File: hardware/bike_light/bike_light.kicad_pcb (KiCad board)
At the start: 2 copper layers, 65 x 22 mm, 54 parts, among them J1 Battery, J2 USB_C_Receptacle_USB2.0_16P, SW1 SW_Push, SW2 SW_Push, U1 TPS22918DBV, U2 ESP32-C3-WROOM-02, U3 XC6220B331MR, U4 BQ21040DBV

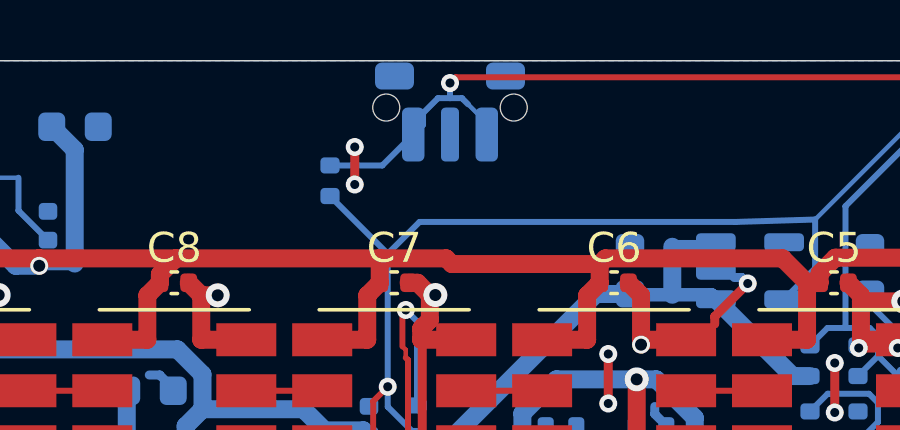
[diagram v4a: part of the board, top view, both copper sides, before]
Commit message: Moved button away from edge a bit
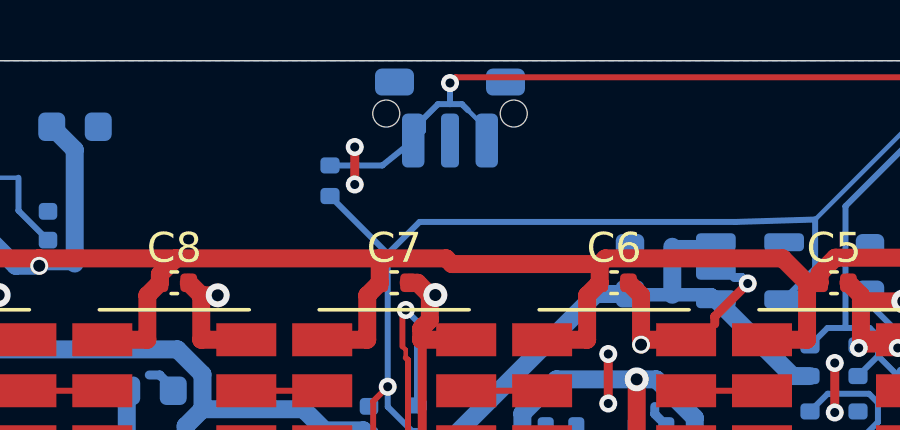
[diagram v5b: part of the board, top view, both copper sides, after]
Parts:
- moved SW1 0.20 mm to (128.0, 101.8)
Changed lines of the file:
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@@
 	(footprint "bike_light:SW_Push_1P1T-MP_NO_Horizontal_Alps_SKRTLAE010"
 		(layer "B.Cu")
-		(at 128 101.56)
+		(at 128 101.76)
 		(descr "Side push button (https://www.alps.com/prod/info/E/PDF/Tact/SurfaceMount/SKRT/SKRT.pdf)")
 		(tags "push horizontal SPST 1P1T")
@@
 	)
 	(segment
-		(start 125.625 114.275)
-		(end 125.275 114.625)
-		(width 0.3)
-		(layer "F.Cu")
-		(net "GND")
-	)
-	(segment
 		(start 155.94 107.4)
 		(end 156.3583 107.8183)
@@
 	)
 	(segment
-		(start 132.575 112.625)
-		(end 132.575 113.325)
-		(width 0.3)
+		(start 156.9883 120.3)
+		(end 158.58 118.7083)
+		(width 0.6)
 		(layer "F.Cu")
 		(net "GND")
 	)
 	(segment
-		(start 122.925 113.975)
-		(end 116.625 113.975)
+		(start 132.125 113.775)
+		(end 129.925 113.775)
 		(width 0.3)
 		(layer "F.Cu")
@@
 	)
 	(segment
-		(start 156.9883 120.3)
-		(end 158.58 118.7083)
-		(width 0.6)
-		(layer "F.Cu")
-		(net "GND")
-	)
-	(segment
 		(start 143.2 109.3)
 		(end 141.6983 109.3)
@@
 	)
 	(segment
+		(start 126.825 114.275)
+		(end 125.625 114.275)
+		(width 0.3)
+		(layer "F.Cu")
+		(net "GND")
+	)
+	(segment
 		(start 151.9487 107.8813)
 		(end 151.9487 107.8812)
@@
 	)
 	(segment
-		(start 124.825 104.125)
-		(end 124.825 102.875)
-		(width 0.3)
-		(layer "F.Cu")
-		(net "GND")
-	)
-	(segment
 		(start 111.96 107.4)
 		(end 112.3783 107.8183)
@@
 	)
 	(segment
-		(start 137.925 107.425)
-		(end 136.825 108.525)
+		(start 122.925 113.975)
+		(end 116.625 113.975)
 		(width 0.3)
 		(layer "F.Cu")
@@
 	)
 	(segment
+		(start 132.575 112.625)
+		(end 132.575 113.325)
+		(width 0.3)
+		(layer "F.Cu")
+		(net "GND")
+	)
+	(segment
 		(start 127.3277 107.8094)
 		(end 127.5114 107.8094)
@@
 	)
 	(segment
+		(start 125.625 114.275)
+		(end 125.275 114.625)
+		(width 0.3)
+		(layer "F.Cu")
+		(net "GND")
+	)
+	(segment
 		(start 135.825 114.925)
 		(end 134.375 116.375)
@@
 	)
 	(segment
+		(start 132.575 113.325)
+		(end 132.125 113.775)
+		(width 0.3)
+		(layer "F.Cu")
+		(net "GND")
+	)
+	(segment
 		(start 105.0483 107.8183)
 		(end 105.0483 109.3)
@@
 	)
 	(segment
-		(start 132.575 113.325)
-		(end 132.125 113.775)
-		(width 0.3)
-		(layer "F.Cu")
-		(net "GND")
-	)
-	(segment
 		(start 156.3583 107.8183)
 		(end 156.3583 109.3)
@@
 	)
 	(segment
-		(start 132.125 113.775)
-		(end 129.925 113.775)
+		(start 137.925 107.425)
+		(end 136.825 108.525)
 		(width 0.3)
 		(layer "F.Cu")
@@
 	)
 	(segment
-		(start 126.825 114.275)
-		(end 125.625 114.275)
+		(start 124.825 104.125)
+		(end 124.825 102.875)
 		(width 0.3)
 		(layer "F.Cu")
@@
 	)
 	(via
-		(at 116.625 113.975)
+		(at 125.275 114.625)
+		(size 0.6)
+		(drill 0.3)
+		(layers "F.Cu" "B.Cu")
+		(net "GND")
+	)
+	(via
+		(at 129.925 113.775)
 		(size 0.6)
 		(drill 0.3)
@@
 	)
 	(via
-		(at 124.825 102.875)
-		(size 0.6)
-		(drill 0.3)
-		(layers "F.Cu" "B.Cu")
-		(net "GND")
-	)
-	(via
-		(at 132.575 112.625)
-		(size 0.6)
-		(drill 0.3)
-		(layers "F.Cu" "B.Cu")
-		(net "GND")
-	)
-	(via
 		(at 122.925 113.975)
 		(size 0.6)
@@
 	)
 	(via
-		(at 127.075 114.125)
+		(at 124.825 104.125)
 		(size 0.6)
 		(drill 0.3)
@@
 	)
 	(via
-		(at 129.925 113.775)
+		(at 132.575 112.625)
 		(size 0.6)
 		(drill 0.3)
@@
 	)
 	(via
-		(at 137.925 107.425)
+		(at 127.075 114.125)
 		(size 0.6)
 		(drill 0.3)
@@
 	)
 	(via
-		(at 125.275 114.625)
-		(size 0.6)
-		(drill 0.3)
+		(at 143.1107 108.0201)
+		(size 0.8)
+		(drill 0.4)
 		(layers "F.Cu" "B.Cu")
 		(net "GND")
 	)
 	(via
-		(at 124.825 104.125)
+		(at 134.375 116.375)
 		(size 0.6)
 		(drill 0.3)
@@
 	)
 	(via
-		(at 143.1107 108.0201)
+		(at 151.9488 107.8812)
 		(size 0.8)
 		(drill 0.4)
@@
 	)
 	(via
-		(at 134.375 116.375)
+		(at 140.825 111.725)
 		(size 0.6)
 		(drill 0.3)
@@
 	)
 	(via
-		(at 151.9488 107.8812)
-		(size 0.8)
-		(drill 0.4)
+		(at 137.925 107.425)
+		(size 0.6)
+		(drill 0.3)
 		(layers "F.Cu" "B.Cu")
 		(net "GND")
 	)
 	(via
-		(at 140.825 111.725)
+		(at 124.825 102.875)
 		(size 0.6)
 		(drill 0.3)
@@
 	)
 	(via
+		(at 116.625 113.975)
+		(size 0.6)
+		(drill 0.3)
+		(layers "F.Cu" "B.Cu")
+		(net "GND")
+	)
+	(via
 		(at 151.275 116.775)
 		(size 0.6)
@@
 	)
 	(segment
-		(start 135.025 111.975)
-		(end 134.825 111.775)
+		(start 137.725 107.225)
+		(end 137.925 107.425)
 		(width 0.3)
 		(layer "B.Cu")
@@
 	)
 	(segment
-		(start 137.475 107.225)
-		(end 137.725 107.225)
+		(start 134.825 111.775)
+		(end 134.825 111.525)
 		(width 0.3)
 		(layer "B.Cu")
@@
 	)
 	(segment
-		(start 125.275 114.625)
-		(end 124.625 113.975)
+		(start 132.825 112.625)
+		(end 132.575 112.625)
 		(width 0.3)
 		(layer "B.Cu")
@@
 	)
 	(segment
-		(start 118.475 110.625)
-		(end 118.325 110.475)
+		(start 135.025 111.975)
+		(end 134.825 111.775)
 		(width 0.3)
 		(layer "B.Cu")
@@
 	)
 	(segment
-		(start 137.725 107.225)
-		(end 137.925 107.425)
+		(start 118.325 110.475)
+		(end 117.975 110.475)
 		(width 0.3)
 		(layer "B.Cu")
@@
 	)
 	(segment
-		(start 134.825 111.775)
-		(end 134.825 111.525)
+		(start 124.625 113.975)
+		(end 122.925 113.975)
 		(width 0.3)
 		(layer "B.Cu")
@@
 	)
 	(segment
-		(start 118.325 110.475)
-		(end 117.975 110.475)
+		(start 118.475 110.625)
+		(end 118.325 110.475)
 		(width 0.3)
 		(layer "B.Cu")
@@
 	)
 	(segment
-		(start 124.625 113.975)
-		(end 122.925 113.975)
+		(start 137.475 107.225)
+		(end 137.725 107.225)
 		(width 0.3)
 		(layer "B.Cu")
@@
 	)
 	(segment
-		(start 132.825 112.625)
-		(end 132.575 112.625)
+		(start 125.275 114.625)
+		(end 124.625 113.975)
 		(width 0.3)
 		(layer "B.Cu")
@@
 	)
 	(segment
-		(start 137.5132 105.3732)
-		(end 140.1715 105.2926)
-		(width 0.2)
-		(layer "B.Cu")
-		(net "+3.3V")
-	)
-	(segment
 		(start 125.9243 110.8658)
 		(end 125.9243 111.5343)
@@
 	)
 	(segment
+		(start 137.5132 105.3732)
+		(end 140.1715 105.2926)
+		(width 0.2)
+		(layer "B.Cu")
+		(net "+3.3V")
+	)
+	(segment
 		(start 143.1426 108.8365)
 		(end 143.452 108.8365)
@@
 	)
 	(segment
-		(start 128 101.246)
-		(end 128.3966 101.246)
+		(start 128 101.446)
+		(end 128.3966 101.446)
 		(width 0.2)
 		(layer "B.Cu")
@@
 	)
 	(segment
-		(start 128.6008 101.4502)
-		(end 129.225 102.0744)
+		(start 128.6008 101.6502)
+		(end 129.225 102.2744)
 		(width 0.15)
 		(layer "B.Cu")
@@
 	)
 	(segment
-		(start 127.1011 101.7459)
-		(end 127.601 101.246)
+		(start 127.1011 101.9459)
+		(end 127.601 101.446)
 		(width 0.2)
 		(layer "B.Cu")
@@
 	)
 	(segment
-		(start 126.775 102.46)
-		(end 127.1011 102.1339)
+		(start 126.775 102.66)
+		(end 127.1011 102.3339)
 		(width 0.2)
 		(layer "B.Cu")
@@
 	)
 	(segment
-		(start 127.601 101.246)
-		(end 128 101.246)
+		(start 127.601 101.446)
+		(end 128 101.446)
 		(width 0.2)
 		(layer "B.Cu")
@@
 	(segment
 		(start 128 100.7417)
-		(end 128 101.246)
+		(end 128 101.446)
 		(width 0.2)
 		(layer "B.Cu")
@@
 	)
 	(segment
-		(start 127.1011 102.1339)
-		(end 127.1011 101.7459)
+		(start 127.1011 102.3339)
+		(end 127.1011 101.9459)
 		(width 0.2)
 		(layer "B.Cu")
@@
 	)
 	(segment
-		(start 129.225 102.0744)
-		(end 129.225 102.46)
+		(start 129.225 102.2744)
+		(end 129.225 102.66)
 		(width 0.15)
 		(layer "B.Cu")
@@
 	)
 	(segment
-		(start 128.3966 101.246)
-		(end 128.6008 101.4502)
+		(start 128.3966 101.446)
+		(end 128.6008 101.6502)
 		(width 0.2)
 		(layer "B.Cu")
@@
 	(segment
 		(start 125.745 103.49)
-		(end 126.775 102.46)
+		(end 126.775 102.66)
 		(width 0.2)
 		(layer "B.Cu")
